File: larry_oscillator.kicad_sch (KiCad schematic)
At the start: 8 parts, among them U1 ${SIM.PARAMS}, U2 ${SIM.PARAMS}

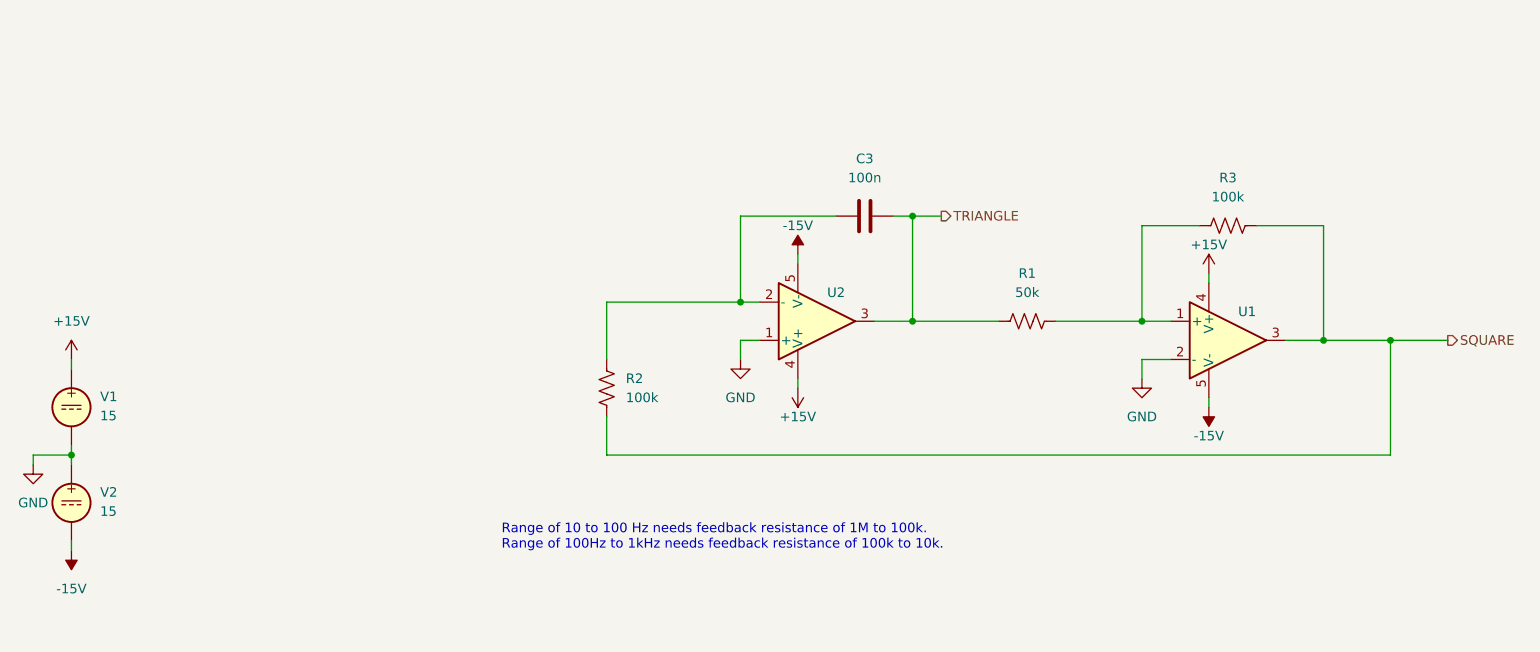
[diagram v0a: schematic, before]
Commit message: added spice model and reworked output stage
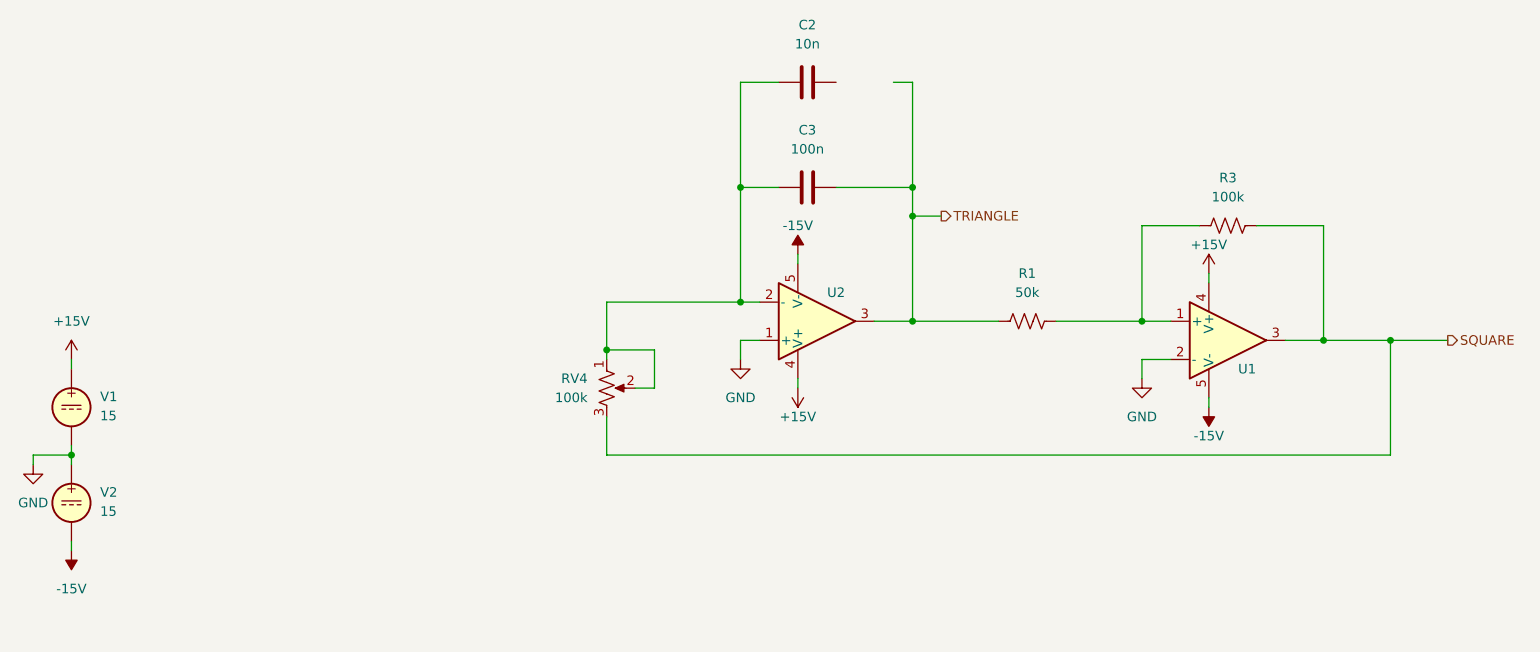
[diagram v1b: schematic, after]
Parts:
- removed R2: 100k, symbol Device:R_US
- added C2: 10n, symbol Device:C
- added RV4: 100k, symbol Device:R_Potentiometer_US
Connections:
- net SQUARE: now also RV4.3
- net at C3.1, U2.2 (-): now also C2.1, RV4.1, RV4.2
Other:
- note removed: "Range of 10 to 100 Hz needs feedback resistance of 1M to 100k. Range of 100Hz to 1kHz needs feedback resistance of 100k to 10k."
- moved on the sheet: C3

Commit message: added pulse gen and other stuff
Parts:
- removed V1, V2: 15, symbol Simulation_SPICE:VDC

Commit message: post wed changes
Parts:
- added Q8: NPN, symbol Simulation_SPICE:NPN
- added R21: 1k, symbol Device:R_US
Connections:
- net GATE: now also R21.1
- net GND: now also Q8.3 (E)
- net TRIANGLE: now also Q8.1 (C)
- new net: Q8.2 (B), R21.2
